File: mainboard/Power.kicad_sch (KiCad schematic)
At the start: 51 parts, among them J2 Power sw, J3 Power LED, J4 ATX-20, U10 74LS00, U14 74LS00, U15 74LS04, U16 74LS74, U18 74LS00, U19 LM7905_TO220, U20 74LS04, U21 74LS04, U22 74LS32, U3 74LS04, U4 74LS32, U6 74LS03, U9 74LS32

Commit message: PCB routed
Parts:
- removed U22: 74LS32, Package_DIP:DIP-14_W7.62mm_LongPads, symbol 74xx:74LS32
- added H1, H10, H2, H3, H4, H5, H6, H7, H8, H9: MountingHole, MountingHole:MountingHole_3.2mm_M3, symbol Mechanical:MountingHole
- added U7: 74LS32, Package_DIP:DIP-14_W7.62mm_Socket_LongPads, symbol 74xx:74LS32
- J2, J3: footprint (none) -> Connector_PinHeader_2.54mm:PinHeader_1x02_P2.54mm_Vertical
- J4: footprint (none) -> Library:ATX_20
- U10, U14, U15, U16, U18, U20, U21, U3, U4, U6: footprint Package_DIP:DIP-14_W7.62mm_LongPads -> Package_DIP:DIP-14_W7.62mm_Socket_LongPads
- U19: footprint (none) -> Package_TO_SOT_THT:TO-220-3_Vertical
- U9: footprint Package_DIP:DIP-16_W7.62mm_LongPads -> Package_DIP:DIP-14_W7.62mm_Socket_LongPads
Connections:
- net +5V: now also U7.14 (VCC)
- net GND: now also U7.7 (GND)

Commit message: unicorn work
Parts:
- removed U7: 74LS32, Package_DIP:DIP-14_W7.62mm_Socket_LongPads, symbol 74xx:74LS32
- added U7: 74LS08, Package_DIP:DIP-14_W7.62mm_Socket_LongPads, symbol 74xx:74LS08
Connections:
- net +5V: now also U7.14 (VCC)
- net GND: now also U7.7 (GND)

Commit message: unicorn work
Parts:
- added C15, C16, C17, C18, C20, C21: 100µF, Capacitor_THT:CP_Radial_D7.5mm_P2.50mm, symbol Device:C_Polarized
- added C48, C50: 0.1µF, Capacitor_THT:C_Rect_L7.0mm_W2.0mm_P5.00mm, symbol Device:C_Small
- renumbered C15 to C19, C16 to C22, C17 to C23, C18 to C24, C19 to C25, C20 to C26, C21 to C27, C22 to C28, C23 to C29, C24 to C30, C25 to C31, C26 to C32, C27 to C33, C28 to C34, C29 to C35, C30 to C36, C31 to C37, C32 to C38, C33 to C39, C34 to C40, C35 to C41, C36 to C42, C37 to C43, C38 to C44, C39 to C45, C40 to C46, C41 to C47, C42 to C49
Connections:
- net +5V: now also C15.1, C16.1, C17.1, C18.1, C20.1, C21.1, C48.1, C50.1
- net GND: now also C15.2, C16.2, C17.2, C18.2, C20.2, C21.2, C48.2, C50.2
- net +3V3: no longer names the net of J4.1 (+3.3V), J4.11 (+3.3V), J4.2 (+3.3V)
- no-connect marks 8 -> 9

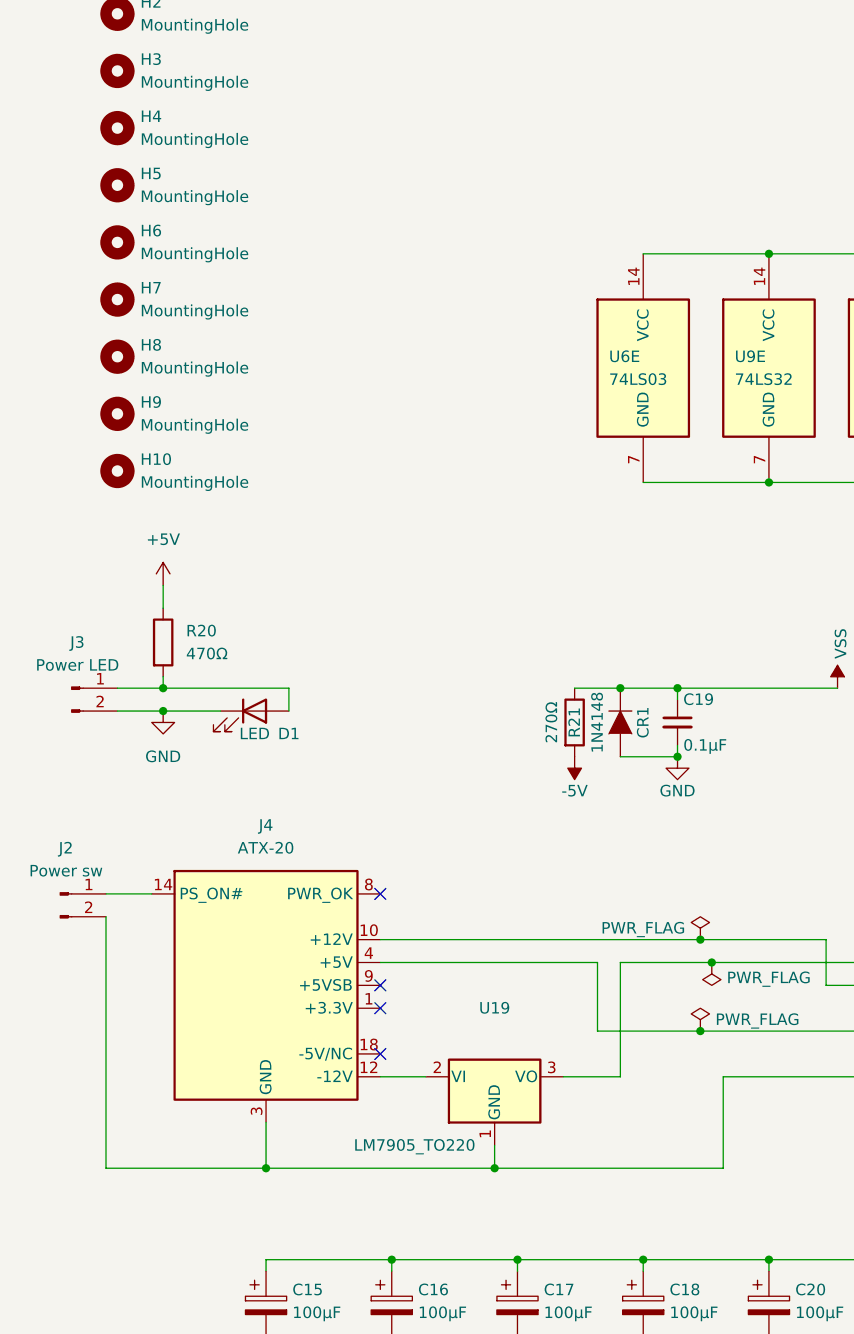
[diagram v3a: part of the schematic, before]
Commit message: Shrink PCB
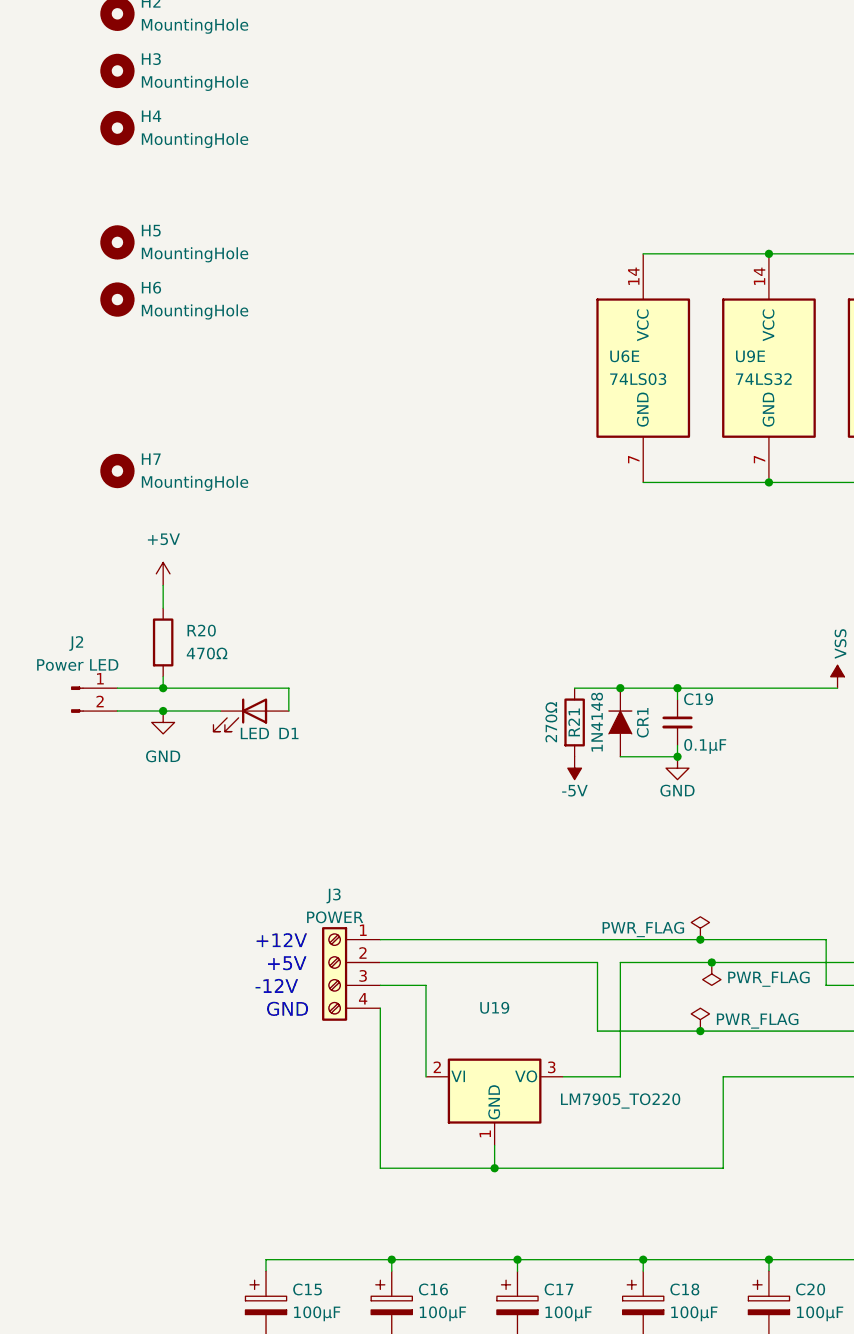
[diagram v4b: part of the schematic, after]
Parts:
- removed H5, H8, H9: MountingHole, MountingHole:MountingHole_3.2mm_M3, symbol Mechanical:MountingHole
- removed J2: Power sw, Connector_PinHeader_2.54mm:PinHeader_1x02_P2.54mm_Vertical, symbol Connector:Conn_01x02_Male
- removed J4: ATX-20, Library:ATX_20, symbol Connector:ATX-20
- added J3: POWER, TerminalBlock_RND:TerminalBlock_RND_205-00278_1x04_P5.00mm_Vertical, symbol Connector:Screw_Terminal_01x04
- renumbered H6 to H5, H7 to H6, H10 to H7, J3 to J2
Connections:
- net +12VIN: now also J3.1 (Pin_1)
- net +5VIN: now also J3.2 (Pin_2)
- net GND: now also J3.4 (Pin_4)
- net at U19.2 (VI): now also J3.3 (Pin_3)
- no-connect marks 9 -> 5
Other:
- note added: "+12V"
- note added: "+5V"
- note added: "-12V"
- note added: "GND"

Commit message: hardware updates
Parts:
- removed L7: 6.8µH, Resistor_THT:R_Axial_DIN0207_L6.3mm_D2.5mm_P7.62mm_Horizontal, symbol Console-rescue:INDUCTOR_SMALL
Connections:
- net +5VIN is gone; now on net +5V: J3.2 (Pin_2)
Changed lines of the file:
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@@
-    (stroke (width 0) (type default) (color 0 0 0 0))
-  )
-  (wire (pts (xy 93.98 147.32) (xy 121.92 147.32))
     (stroke (width 0) (type default) (color 0 0 0 0))
   )
@@
     (stroke (width 0) (type default) (color 0 0 0 0))
   )
-  (wire (pts (xy 134.62 147.32) (xy 138.43 147.32))
+  (wire (pts (xy 93.98 147.32) (xy 138.43 147.32))
     (stroke (width 0) (type default) (color 0 0 0 0))
   )
@@
     )
     (pin "1")
-    (pin "2")
-  )
-  (symbol (lib_id "Console-rescue:INDUCTOR_SMALL") (at 128.27 147.32 0) (mirror y) (unit 1)
-    (in_bom yes) (on_board yes)
-    (property "Reference" "L7" (id 0) (at 124.46 144.78 0))
-    (property "Value" "6.8µH" (id 1) (at 132.08 144.78 0))
-    (property "Footprint" "Resistor_THT:R_Axial_DIN0207_L6.3mm_D2.5mm_P7.62mm_Horizontal" (id 2) (at 128.27 147.32 0)
-      (effects (font (size 1.524 1.524)) hide)
-    )
-    (property "Datasheet" "" (id 3) (at 128.27 147.32 0)
-      (effects (font (size 1.524 1.524)))
-    )
-    (pin "1")

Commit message: hardware updates
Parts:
- renumbered R20 to R19, R21 to R20
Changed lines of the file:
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@@
   (symbol (lib_id "Device:R") (at 34.29 104.14 0) (unit 1)
     (in_bom yes) (on_board yes) (fields_autoplaced)
-    (property "Reference" "R20" (id 0) (at 36.83 102.8699 0)
+    (property "Reference" "R19" (id 0) (at 36.83 102.8699 0)
       (effects (font (size 1.27 1.27)) (justify left))
     )
@@
   (symbol (lib_id "Console-rescue:R") (at 80.01 113.03 0) (unit 1)
     (in_bom yes) (on_board yes)
-    (property "Reference" "R21" (id 0) (at 80.01 113.03 90))
+    (property "Reference" "R20" (id 0) (at 80.01 113.03 90))
     (property "Value" "270Ω" (id 1) (at 77.47 113.03 90))
     (property "Footprint" "Resistor_THT:R_Axial_DIN0207_L6.3mm_D2.5mm_P7.62mm_Horizontal" (id 2) (at 78.232 113.03 90)

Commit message: PCB cleanup
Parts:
- added U21: RC4558, Package_DIP:DIP-8_W7.62mm_Socket_LongPads, symbol Amplifier_Operational:RC4558
- C19: symbol TI-Customs:C_Small -> Device:C
- CR1: symbol Console-rescue:D -> Device:D
- L5, L6: symbol Console-rescue:INDUCTOR_SMALL -> Device:L
- R20: symbol Console-rescue:R -> Device:R
- renumbered U21 to U22
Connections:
- net +5V: now also U21.8 (V+)
- net -5V: now also U21.4 (V-)
- net +12VIN: no longer names the net of J3.1 (Pin_1), L6.2
- net -5VIN: no longer names the net of L5.2, U19.3 (VO)
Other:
- moved on the sheet: L5, L6

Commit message: PCB rework
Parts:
- added C18: 0.1µF, Capacitor_THT:C_Rect_L7.0mm_W2.0mm_P5.00mm, symbol Device:C_Small
- added U19: LM2901, Package_DIP:DIP-14_W7.62mm_Socket_LongPads, symbol Comparator:LM2901
- added U21: LM2903, Package_DIP:DIP-8_W7.62mm_Socket_LongPads, symbol Comparator:LM2903
- added U47: 74LS06, Package_DIP:DIP-14_W7.62mm_Socket_LongPads, symbol 74xx:74LS06
- L4: renamed from L5; footprint Resistor_THT:R_Axial_DIN0207_L6.3mm_D2.5mm_P7.62mm_Horizontal -> Resistor_THT:R_Axial_DIN0207_L6.3mm_D2.5mm_P15.24mm_Horizontal
- L5: renamed from L6; footprint Resistor_THT:R_Axial_DIN0207_L6.3mm_D2.5mm_P7.62mm_Horizontal -> Resistor_THT:R_Axial_DIN0207_L6.3mm_D2.5mm_P15.24mm_Horizontal
- renumbered C18 to C19, C19 to C20, C20 to C21, C21 to C22, C22 to C23, C23 to C24, C24 to C25, C25 to C26, C26 to C27, C27 to C28, C28 to C29, C29 to C30, C30 to C31, C31 to C32, C32 to C33, C33 to C34, C34 to C35, C35 to C36, C36 to C37, C37 to C38, C38 to C39, C39 to C40, C40 to C41, C41 to C42, C42 to C43, C43 to C44, C44 to C45, C45 to C46, C46 to C47, C47 to C48, C48 to C49, C49 to C50, C50 to C51, U19 to U20, U20 to U22, U22 to U24, U21 to U46
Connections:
- net +5V: now also C18.1, U19.3 (V+), U21.8 (V+), U47.14 (VCC)
- net GND: now also C18.2, U19.12 (V-), U21.4 (V-), U47.7 (GND)
- no-connect marks 5 -> 7
